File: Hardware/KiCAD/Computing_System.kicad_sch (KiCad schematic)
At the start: 2 parts, among them IC1 ESP32-C3-WROOM-02-N4, J1 SD_Card

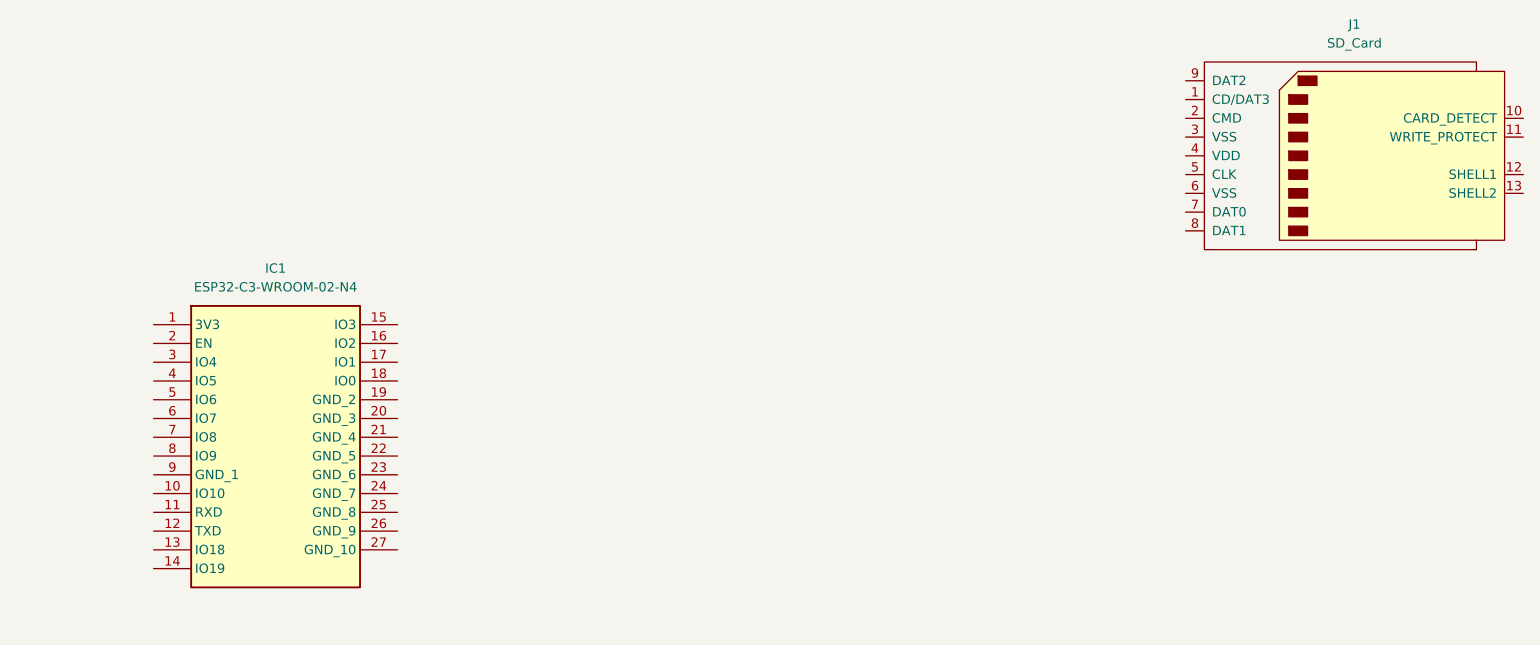
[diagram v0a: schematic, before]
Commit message: feat: Connect ESP32 to CC1200
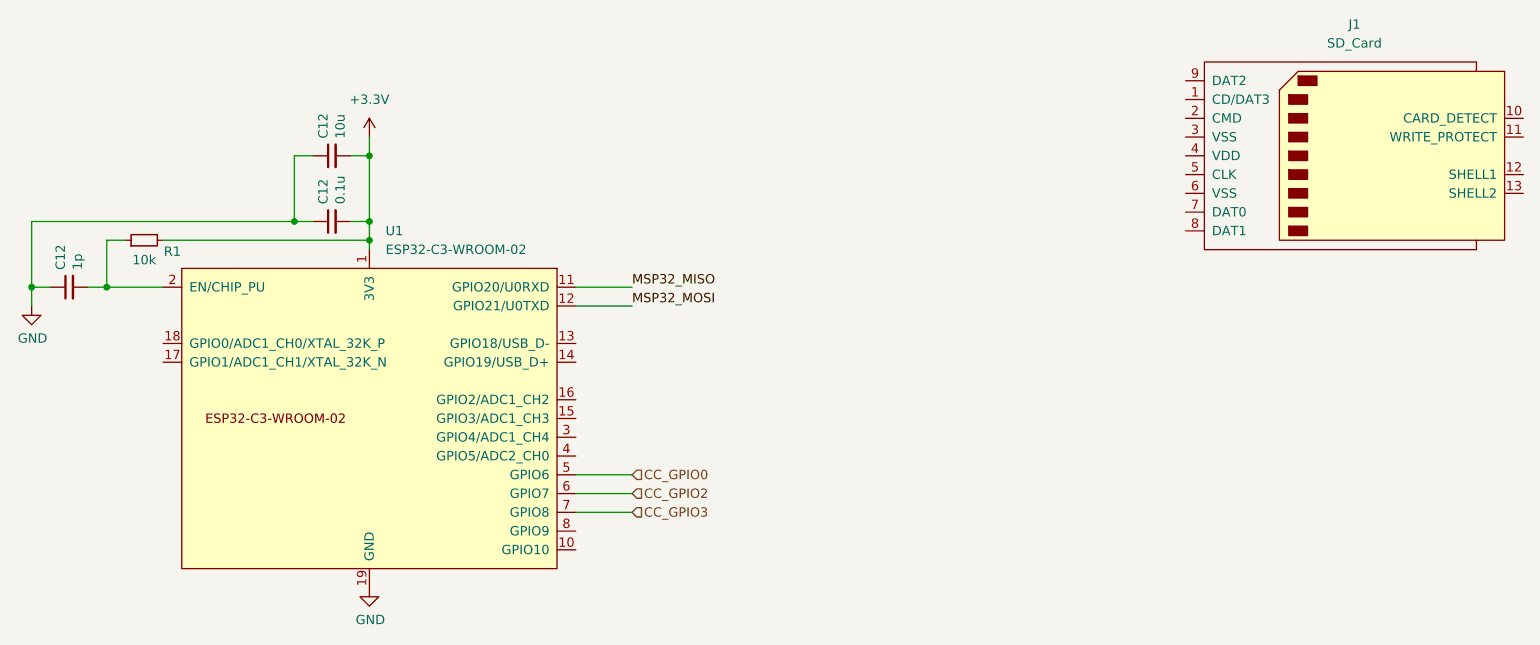
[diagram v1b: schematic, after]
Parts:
- removed IC1: ESP32-C3-WROOM-02-N4, Cobalt_Cowboy:ESP32C3WROOM02N4, symbol Cobalt_Cowboy:ESP32-C3-WROOM-02-N4
- added C12: 0.1u, Capacitor_SMD:C_0402_1005Metric, symbol pkl_device:pkl_C_Small
- added C12: 10u, Capacitor_SMD:C_0402_1005Metric, symbol pkl_device:pkl_C_Small
- added C12: 1p, Capacitor_SMD:C_0402_1005Metric, symbol pkl_device:pkl_C_Small
- added R1: 10k, Resistor_SMD:R_0402_1005Metric, symbol pkl_device:pkl_R_Small
- added U1: ESP32-C3-WROOM-02, PCM_Espressif:ESP32-C3-WROOM-02, symbol PCM_Espressif:ESP32-C3-WROOM-02
- J1: footprint (none) -> Connector_Card:microSD_HC_Hirose_DM3AT-SF-PEJM5
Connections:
- new net: C12.2, R1.1, U1.2 (EN/CHIP_PU)
- new net +3.3V: C12.2, C12.2, R1.2, U1.1 (3V3)
- new net CC_GPIO0: U1.5 (GPIO6)
- new net CC_GPIO2: U1.6 (GPIO7)
- new net CC_GPIO3: U1.7 (GPIO8)
- new net GND: C12.1, C12.1, C12.1, U1.19 (GND), U1.9 (GND)
- new net MSP32_MISO: U1.11 (GPIO20/U0RXD)
- new net MSP32_MOSI: U1.12 (GPIO21/U0TXD)

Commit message: feat: add models, correct hierarchical patterns
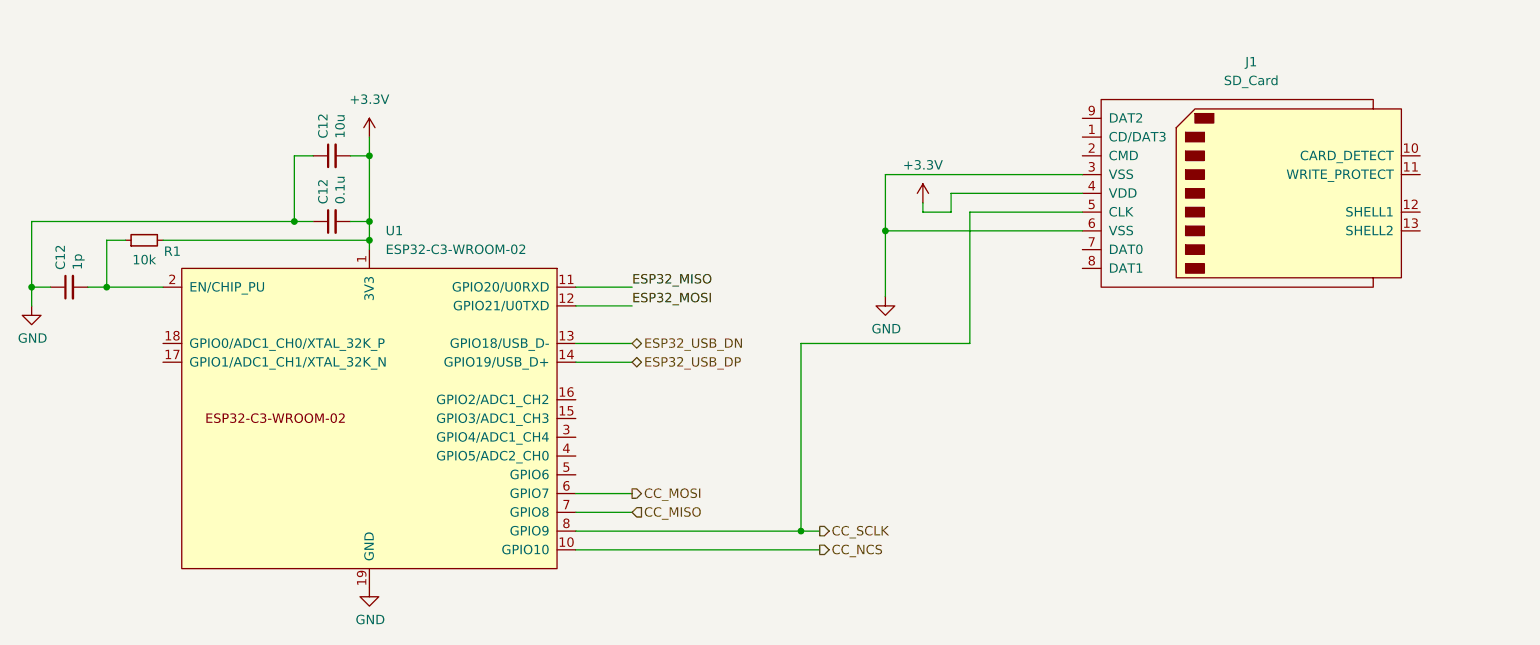
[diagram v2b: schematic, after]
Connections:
- net +3.3V: now also J1.4 (VDD)
- net GND: now also J1.3 (VSS), J1.6 (VSS)
- net CC_SCLK: now reaches J1.5 (CLK)
- net CC_SCLK: now also U1.8 (GPIO9)
- net CC_NCS: now reaches U1.10 (GPIO10)
- net ESP32_USB_DN: now reaches U1.13 (GPIO18/USB_D-)
- net ESP32_USB_DP: now reaches U1.14 (GPIO19/USB_D+)
- net CC_GPIO0: no longer names the net of U1.5 (GPIO6)
- net CC_GPIO2 renamed CC_MOSI
- net CC_GPIO3 renamed CC_MISO
- net MSP32_MISO renamed ESP32_MISO
- net MSP32_MOSI renamed ESP32_MOSI
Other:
- moved on the sheet: J1
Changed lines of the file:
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@@
   (junction (at 121.92 48.26) (diameter 0) (color 0 0 0 0)
   )
+  (junction (at 180.34 90.17) (diameter 0) (color 0 0 0 0)
+  )
+  (junction (at 191.77 49.53) (diameter 0) (color 0 0 0 0)
+  )
+  (wire (pts (xy 218.44 46.99) (xy 203.2 46.99))
+    (stroke (width 0) (type default))
+  )
   (wire (pts (xy 121.92 39.37) (xy 121.92 48.26))
     (stroke (width 0) (type default))
@@
     (stroke (width 0) (type default))
   )
-  (wire (pts (xy 157.48 85.09) (xy 149.86 85.09))
+  (wire (pts (xy 191.77 49.53) (xy 218.44 49.53))
+    (stroke (width 0) (type default))
+  )
+  (wire (pts (xy 200.66 46.99) (xy 200.66 44.45))
+    (stroke (width 0) (type default))
+  )
+  (wire (pts (xy 149.86 67.31) (xy 157.48 67.31))
+    (stroke (width 0) (type default))
+  )
+  (wire (pts (xy 191.77 41.91) (xy 191.77 49.53))
     (stroke (width 0) (type default))
   )
@@
     (stroke (width 0) (type default))
   )
+  (wire (pts (xy 149.86 90.17) (xy 180.34 90.17))
+    (stroke (width 0) (type default))
+  )
   (wire (pts (xy 88.9 50.8) (xy 86.36 50.8))
     (stroke (width 0) (type default))
   )
+  (wire (pts (xy 196.85 45.72) (xy 196.85 46.99))
+    (stroke (width 0) (type default))
+  )
+  (wire (pts (xy 191.77 49.53) (xy 191.77 58.42))
+    (stroke (width 0) (type default))
+  )
+  (wire (pts (xy 203.2 46.99) (xy 203.2 64.77))
+    (stroke (width 0) (type default))
+  )
   (wire (pts (xy 93.98 50.8) (xy 121.92 50.8))
     (stroke (width 0) (type default))
   )
+  (wire (pts (xy 180.34 90.17) (xy 182.88 90.17))
+    (stroke (width 0) (type default))
+  )
   (wire (pts (xy 76.2 48.26) (xy 76.2 57.15))
     (stroke (width 0) (type default))
@@
     (stroke (width 0) (type default))
   )
+  (wire (pts (xy 180.34 64.77) (xy 180.34 90.17))
+    (stroke (width 0) (type default))
+  )
   (wire (pts (xy 114.3 39.37) (xy 111.76 39.37))
     (stroke (width 0) (type default))
@@
     (stroke (width 0) (type default))
   )
-  (wire (pts (xy 157.48 87.63) (xy 149.86 87.63))
+  (wire (pts (xy 200.66 44.45) (xy 218.44 44.45))
+    (stroke (width 0) (type default))
+  )
+  (wire (pts (xy 218.44 41.91) (xy 191.77 41.91))
+    (stroke (width 0) (type default))
+  )
+  (wire (pts (xy 149.86 85.09) (xy 157.48 85.09))
     (stroke (width 0) (type default))
   )
@@
     (stroke (width 0) (type default))
   )
+  (wire (pts (xy 149.86 87.63) (xy 157.48 87.63))
+    (stroke (width 0) (type default))
+  )
+  (wire (pts (xy 149.86 64.77) (xy 157.48 64.77))
+    (stroke (width 0) (type default))
+  )
+  (wire (pts (xy 203.2 64.77) (xy 180.34 64.77))
+    (stroke (width 0) (type default))
+  )
   (wire (pts (xy 111.76 48.26) (xy 76.2 48.26))
     (stroke (width 0) (type default))
@@
     (stroke (width 0) (type default))
   )
+  (wire (pts (xy 196.85 46.99) (xy 200.66 46.99))
+    (stroke (width 0) (type default))
+  )
   (wire (pts (xy 121.92 36.83) (xy 121.92 39.37))
     (stroke (width 0) (type default))
@@
     (stroke (width 0) (type default))
   )
+  (wire (pts (xy 149.86 92.71) (xy 182.88 92.71))
+    (stroke (width 0) (type default))
+  )
   (wire (pts (xy 76.2 57.15) (xy 78.74 57.15))
     (stroke (width 0) (type default))
   )
-  (wire (pts (xy 157.48 82.55) (xy 149.86 82.55))
-    (stroke (width 0) (type default))
-  )
-  (label "MSP32_MISO" (at 157.48 57.15 0) (fields_autoplaced)
+  (label "ESP32_MISO" (at 157.48 57.15 0) (fields_autoplaced)
     (effects (font (size 1.27 1.27)) (justify left bottom))
   )
-  (label "MSP32_MOSI" (at 157.48 59.69 0) (fields_autoplaced)
+  (label "ESP32_MOSI" (at 157.48 59.69 0) (fields_autoplaced)
     (effects (font (size 1.27 1.27)) (justify left bottom))
   )
-  (hierarchical_label "CC_GPIO2" (shape input) (at 157.48 85.09 0) (fields_autoplaced)
-    (effects (font (size 1.27 1.27)) (justify left))
-  )
-  (hierarchical_label "CC_GPIO0" (shape input) (at 157.48 82.55 0) (fields_autoplaced)
-    (effects (font (size 1.27 1.27)) (justify left))
-  )
-  (hierarchical_label "CC_GPIO3" (shape input) (at 157.48 87.63 0) (fields_autoplaced)
+  (hierarchical_label "CC_NCS" (shape output) (at 182.88 92.71 0) (fields_autoplaced)
+    (effects (font (size 1.27 1.27)) (justify left))
+  )
+  (hierarchical_label "ESP32_USB_DP" (shape bidirectional) (at 157.48 67.31 0) (fields_autoplaced)
+    (effects (font (size 1.27 1.27)) (justify left))
+  )
+  (hierarchical_label "CC_MOSI" (shape output) (at 157.48 85.09 0) (fields_autoplaced)
+    (effects (font (size 1.27 1.27)) (justify left))
+  )
+  (hierarchical_label "CC_MISO" (shape input) (at 157.48 87.63 0) (fields_autoplaced)
+    (effects (font (size 1.27 1.27)) (justify left))
+  )
+  (hierarchical_label "CC_SCLK" (shape output) (at 182.88 90.17 0) (fields_autoplaced)
+    (effects (font (size 1.27 1.27)) (justify left))
+  )
+  (hierarchical_label "ESP32_USB_DN" (shape bidirectional) (at 157.48 64.77 0) (fields_autoplaced)
     (effects (font (size 1.27 1.27)) (justify left))
   )
@@
     )
   )
-  (symbol (lib_id "Connector:SD_Card") (at 255.27 39.37 0) (unit 1)
+  (symbol (lib_id "Connector:SD_Card") (at 241.3 44.45 0) (unit 1)
     (in_bom yes) (on_board yes) (dnp no) (fields_autoplaced)
-    (property "Reference" "J1" (at 255.27 21.59 0)
-      (effects (font (size 1.27 1.27)))
-    )
-    (property "Value" "SD_Card" (at 255.27 24.13 0)
-      (effects (font (size 1.27 1.27)))
-    )
-    (property "Footprint" "Connector_Card:microSD_HC_Hirose_DM3AT-SF-PEJM5" (at 255.27 39.37 0)
-      (effects (font (size 1.27 1.27)) hide)
-    )
-    (property "Datasheet" "http://portal.fciconnect.com/Comergent//fci/drawing/10067847.pdf" (at 255.27 39.37 0)
+    (property "Reference" "J1" (at 241.3 26.67 0)
+      (effects (font (size 1.27 1.27)))
+    )
+    (property "Value" "SD_Card" (at 241.3 29.21 0)
+      (effects (font (size 1.27 1.27)))
+    )
+    (property "Footprint" "Connector_Card:microSD_HC_Hirose_DM3AT-SF-PEJM5" (at 241.3 44.45 0)
+      (effects (font (size 1.27 1.27)) hide)
+    )
+    (property "Datasheet" "http://portal.fciconnect.com/Comergent//fci/drawing/10067847.pdf" (at 241.3 44.45 0)
       (effects (font (size 1.27 1.27)) hide)
     )
@@
     )
   )
+  (symbol (lib_id "power:GND") (at 191.77 58.42 0) (unit 1)
+    (in_bom yes) (on_board yes) (dnp no)
+    (property "Reference" "#PWR017" (at 191.77 64.77 0)
+      (effects (font (size 1.27 1.27)) hide)
+    )
+    (property "Value" "GND" (at 191.897 62.8142 0)
+      (effects (font (size 1.27 1.27)))
+    )
+    (property "Footprint" "" (at 191.77 58.42 0)
+      (effects (font (size 1.27 1.27)) hide)
+    )
+    (property "Datasheet" "" (at 191.77 58.42 0)
+      (effects (font (size 1.27 1.27)) hide)
+    )
+    (pin "1")
+    (instances
+      (project "Cobalt-Cowboy"
+        (path "/60a68eb1-aa0f-414e-b03b-965ad6b52dab/d80d452c-0cd9-4253-b692-c2cdb4b1394b"
+          (reference "#PWR017") (unit 1)
+        )
+        (path "/60a68eb1-aa0f-414e-b03b-965ad6b52dab/1039084b-a0e1-47ac-823b-a237cfc3ed39"
+          (reference "#PWR038") (unit 1)
+        )
+      )
+      (project "Mini17"
+        (path "/c89c6552-5574-4959-bcaf-f05dfde21961/f4521ef1-9a41-474d-b880-30e1e54c8ecb"
+          (reference "#PWR035") (unit 1)
+        )
+      )
+    )
+  )
   (symbol (lib_id "pkl_device:pkl_C_Small") (at 81.28 57.15 90) (unit 1)
     (in_bom yes) (on_board yes) (dnp no)
@@
         )
       )
+    )
+  )
+  (symbol (lib_id "power:+3.3V") (at 196.85 45.72 0) (unit 1)
+    (in_bom yes) (on_board yes) (dnp no) (fields_autoplaced)
+    (property "Reference" "#PWR037" (at 196.85 49.53 0)
+      (effects (font (size 1.27 1.27)) hide)
+    )
+    (property "Value" "+3.3V" (at 196.85 40.64 0)
+      (effects (font (size 1.27 1.27)))
+    )
+    (property "Footprint" "" (at 196.85 45.72 0)
+      (effects (font (size 1.27 1.27)) hide)
+    )
+    (property "Datasheet" "" (at 196.85 45.72 0)
+      (effects (font (size 1.27 1.27)) hide)
+    )
+    (pin "1")
+    (instances
+      (project "Cobalt-Cowboy"
+        (path "/60a68eb1-aa0f-414e-b03b-965ad6b52dab/1039084b-a0e1-47ac-823b-a237cfc3ed39"
+          (reference "#PWR037") (unit 1)
+        )
+      )

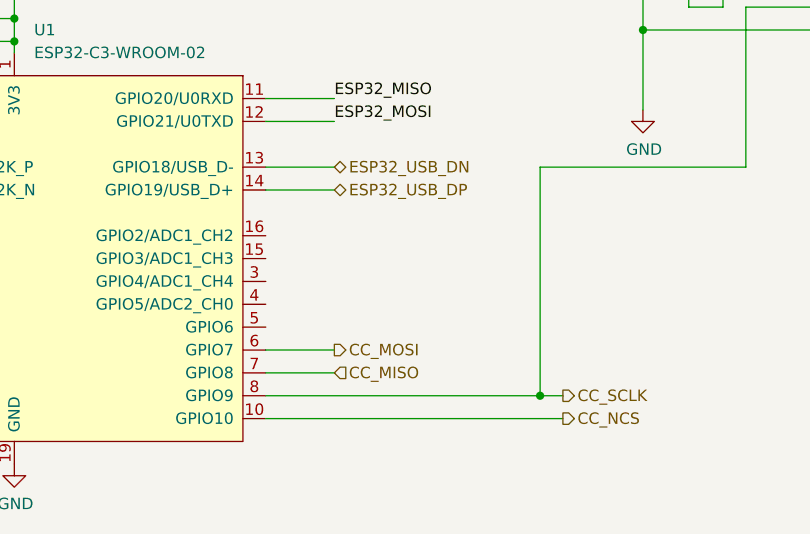
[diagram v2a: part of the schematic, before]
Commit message: fix: revised GPIO pins for CC1200 SPI pins
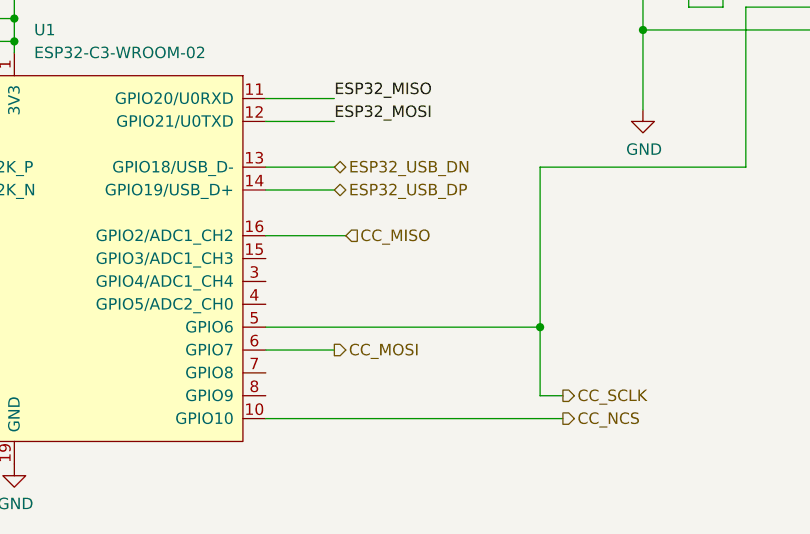
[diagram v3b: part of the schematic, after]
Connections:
- net CC_MISO: now also U1.16 (GPIO2/ADC1_CH2); no longer U1.7 (GPIO8)
- net CC_SCLK: now also U1.5 (GPIO6); no longer U1.8 (GPIO9)
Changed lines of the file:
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@@
   (junction (at 121.92 48.26) (diameter 0) (color 0 0 0 0)
   )
-  (junction (at 180.34 90.17) (diameter 0) (color 0 0 0 0)
+  (junction (at 180.34 82.55) (diameter 0) (color 0 0 0 0)
   )
   (junction (at 191.77 49.53) (diameter 0) (color 0 0 0 0)
@@
     (stroke (width 0) (type default))
   )
-  (wire (pts (xy 149.86 90.17) (xy 180.34 90.17))
-    (stroke (width 0) (type default))
-  )
   (wire (pts (xy 88.9 50.8) (xy 86.36 50.8))
     (stroke (width 0) (type default))
   )
   (wire (pts (xy 196.85 45.72) (xy 196.85 46.99))
+    (stroke (width 0) (type default))
+  )
+  (wire (pts (xy 149.86 72.39) (xy 158.75 72.39))
     (stroke (width 0) (type default))
   )
@@
     (stroke (width 0) (type default))
   )
-  (wire (pts (xy 180.34 64.77) (xy 180.34 90.17))
+  (wire (pts (xy 180.34 64.77) (xy 180.34 82.55))
     (stroke (width 0) (type default))
   )
@@
     (stroke (width 0) (type default))
   )
-  (wire (pts (xy 218.44 41.91) (xy 191.77 41.91))
+  (wire (pts (xy 149.86 85.09) (xy 157.48 85.09))
     (stroke (width 0) (type default))
   )
-  (wire (pts (xy 149.86 85.09) (xy 157.48 85.09))
+  (wire (pts (xy 218.44 41.91) (xy 191.77 41.91))
     (stroke (width 0) (type default))
   )
@@
     (stroke (width 0) (type default))
   )
-  (wire (pts (xy 149.86 87.63) (xy 157.48 87.63))
+  (wire (pts (xy 149.86 64.77) (xy 157.48 64.77))
     (stroke (width 0) (type default))
   )
-  (wire (pts (xy 149.86 64.77) (xy 157.48 64.77))
+  (wire (pts (xy 180.34 82.55) (xy 180.34 90.17))
     (stroke (width 0) (type default))
   )
@@
   )
   (wire (pts (xy 76.2 57.15) (xy 76.2 59.69))
+    (stroke (width 0) (type default))
+  )
+  (wire (pts (xy 149.86 82.55) (xy 180.34 82.55))
     (stroke (width 0) (type default))
   )
@@
     (effects (font (size 1.27 1.27)) (justify left))
   )
-  (hierarchical_label "CC_MISO" (shape input) (at 157.48 87.63 0) (fields_autoplaced)
+  (hierarchical_label "CC_MISO" (shape input) (at 158.75 72.39 0) (fields_autoplaced)
     (effects (font (size 1.27 1.27)) (justify left))
   )
